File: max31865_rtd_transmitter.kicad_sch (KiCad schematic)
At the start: 4 parts, among them U1 MAX31865xTP

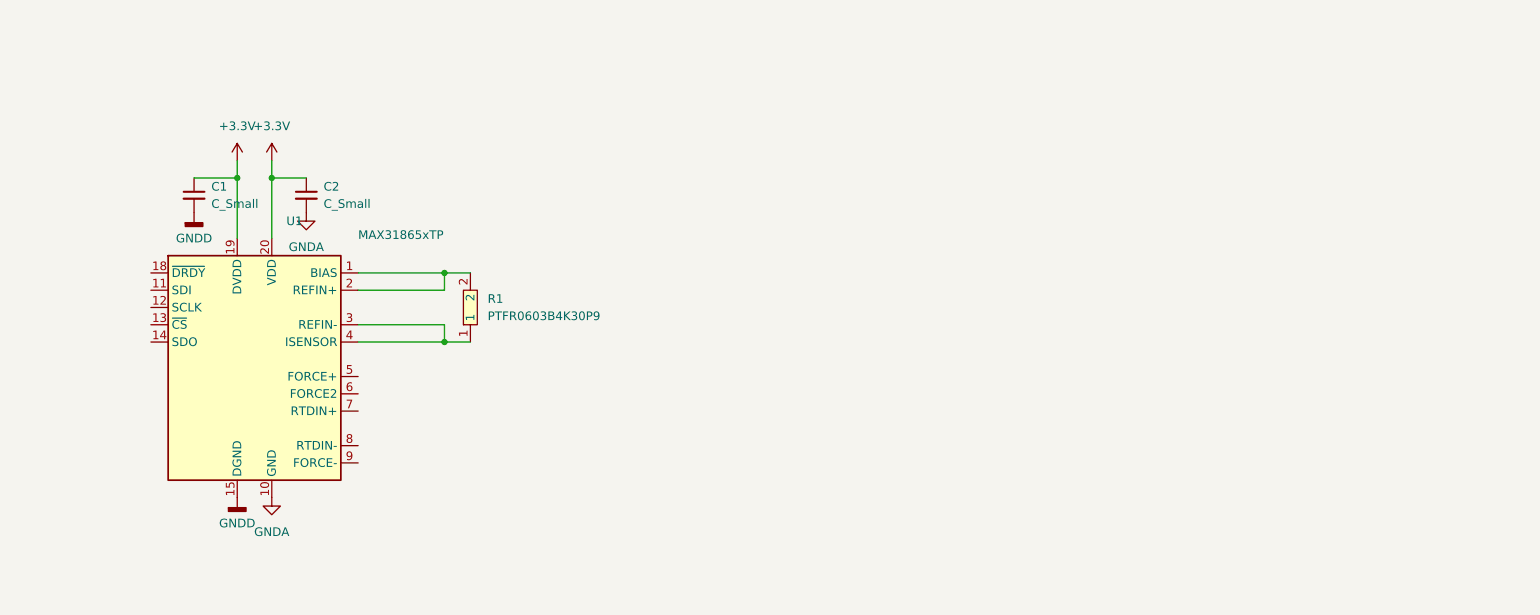
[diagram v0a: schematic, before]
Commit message: Add isolated power and LDO
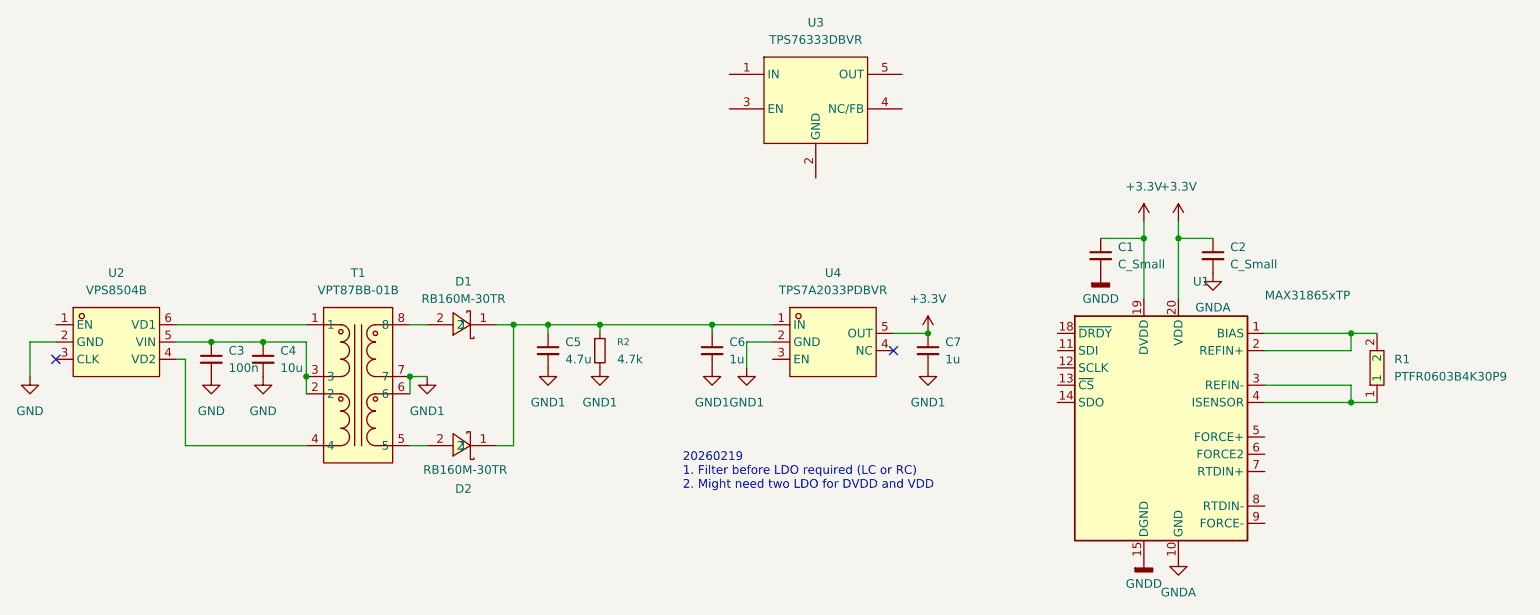
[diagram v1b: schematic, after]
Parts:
- added C3: 100n, symbol Device:C_Small
- added C4: 10u, symbol Device:C_Small
- added C5: 4.7u, symbol Device:C_Small
- added C6, C7: 1u, symbol Device:C_Small
- added D1, D2: RB160M-30TR, rtd-transmitter-library:SOD-123_L2.8-W1.8-LS3.7-RD, symbol rtd-transmitter-library:RB160M-30TR
- added R2: 4.7k, symbol Device:R_Small
- added T1: VPT87BB-01B, rtd-transmitter-library:XFMR-SMD_VPSC_VPT87BB, symbol rtd-transmitter-library:VPT87BB-01B
- added U2: VPS8504B, rtd-transmitter-library:SOT-23-6_L2.9-W1.6-P0.95-LS2.8-BR, symbol rtd-transmitter-library:VPS8504B
- added U3: TPS76333DBVR, rtd-transmitter-library:SOT-23-5_L3.0-W1.7-P0.95-LS2.8-BR, symbol rtd-transmitter-library:TPS76333DBVR
- added U4: TPS7A2033PDBVR, rtd-transmitter-library:SOT-23-5_L2.9-W1.6-P0.95-LS2.8-BR, symbol rtd-transmitter-library:TPS7A2033PDBVR
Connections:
- net +3.3V: now also C7.1, U4.5 (OUT)
- new net: C5.1, C6.1, D1.1, D2.1, R2.1, U4.1 (IN)
- new net: C3.1, C4.1, T1.2, T1.3, U2.5 (VIN)
- new net: T1.1, U2.6 (VD1)
- new net: T1.4, U2.4 (VD2)
- new net: D2.2, T1.5
- new net: D1.2, T1.8
- new net GND: C3.2, C4.2, U2.2 (GND)
- new net GND1: C5.2, C6.2, C7.2, R2.2, T1.6, T1.7, U4.2 (GND)
- no-connect marks 0 -> 2
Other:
- note added: "20260219 1. Filter before LDO required (LC or RC) 2. Might need two LDO for DVDD and VDD"
- moved on the sheet: C1, C2, R1, U1

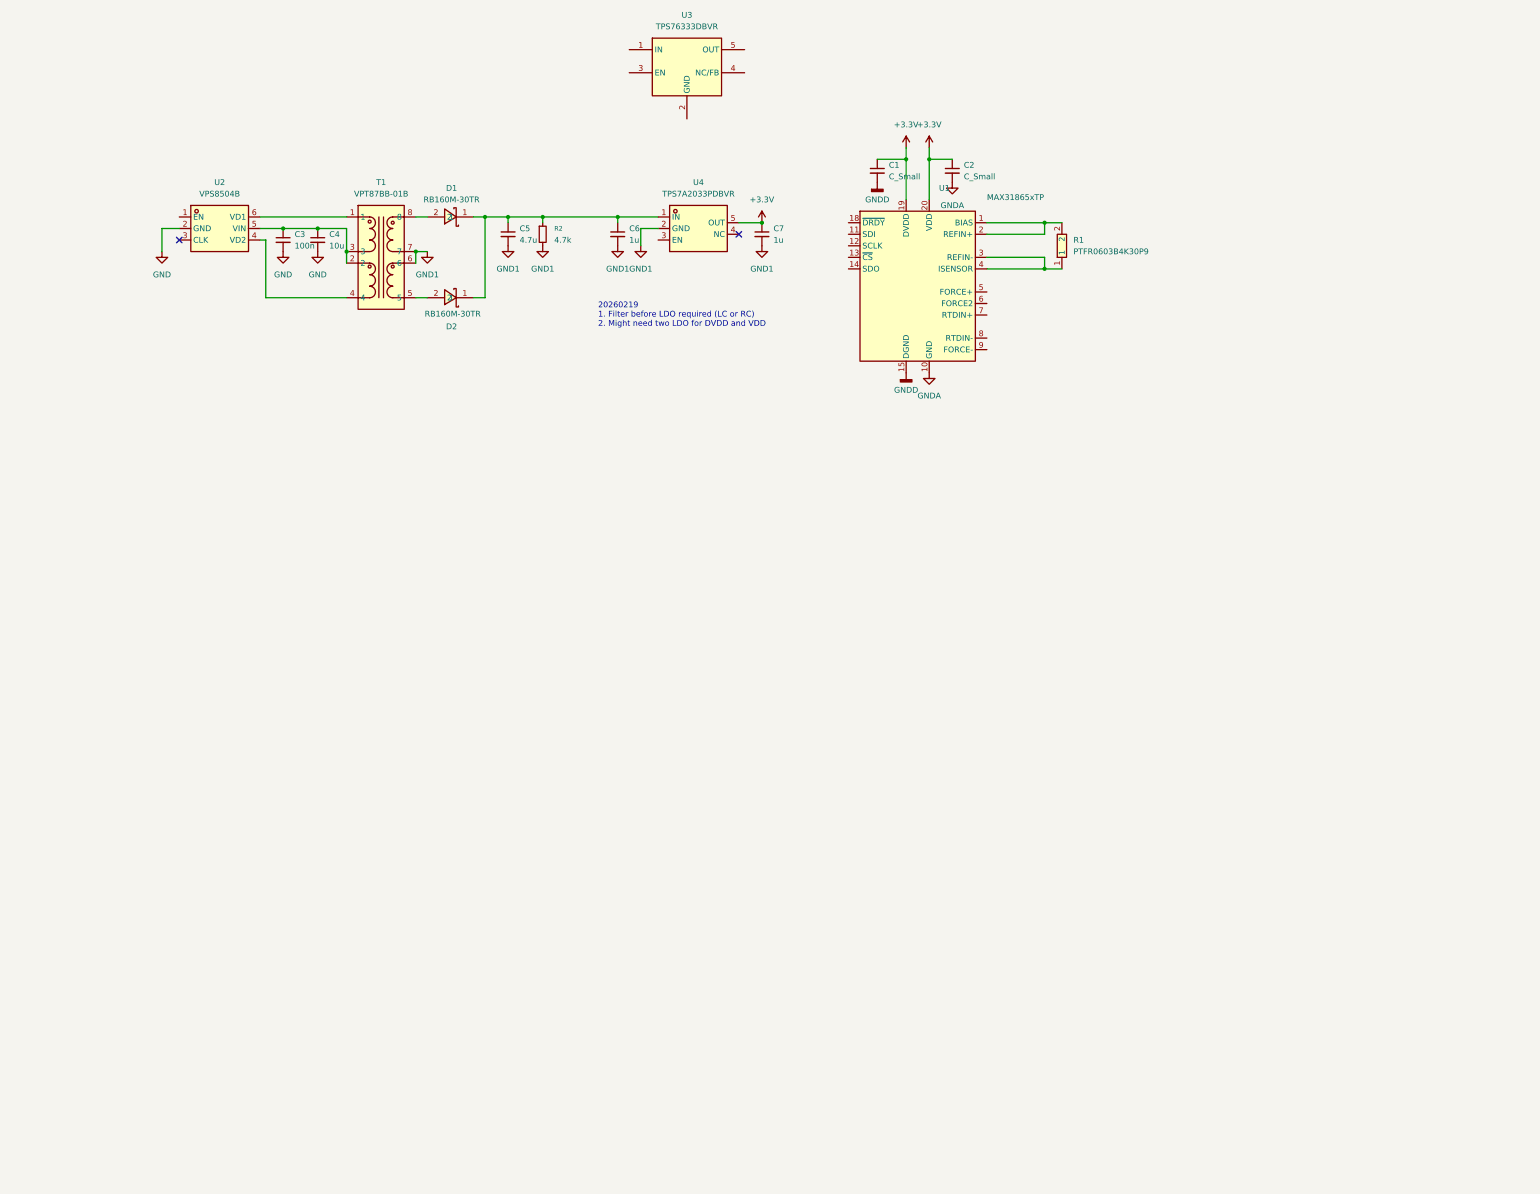
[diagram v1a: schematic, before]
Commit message: Complete single channel design, add rp2350
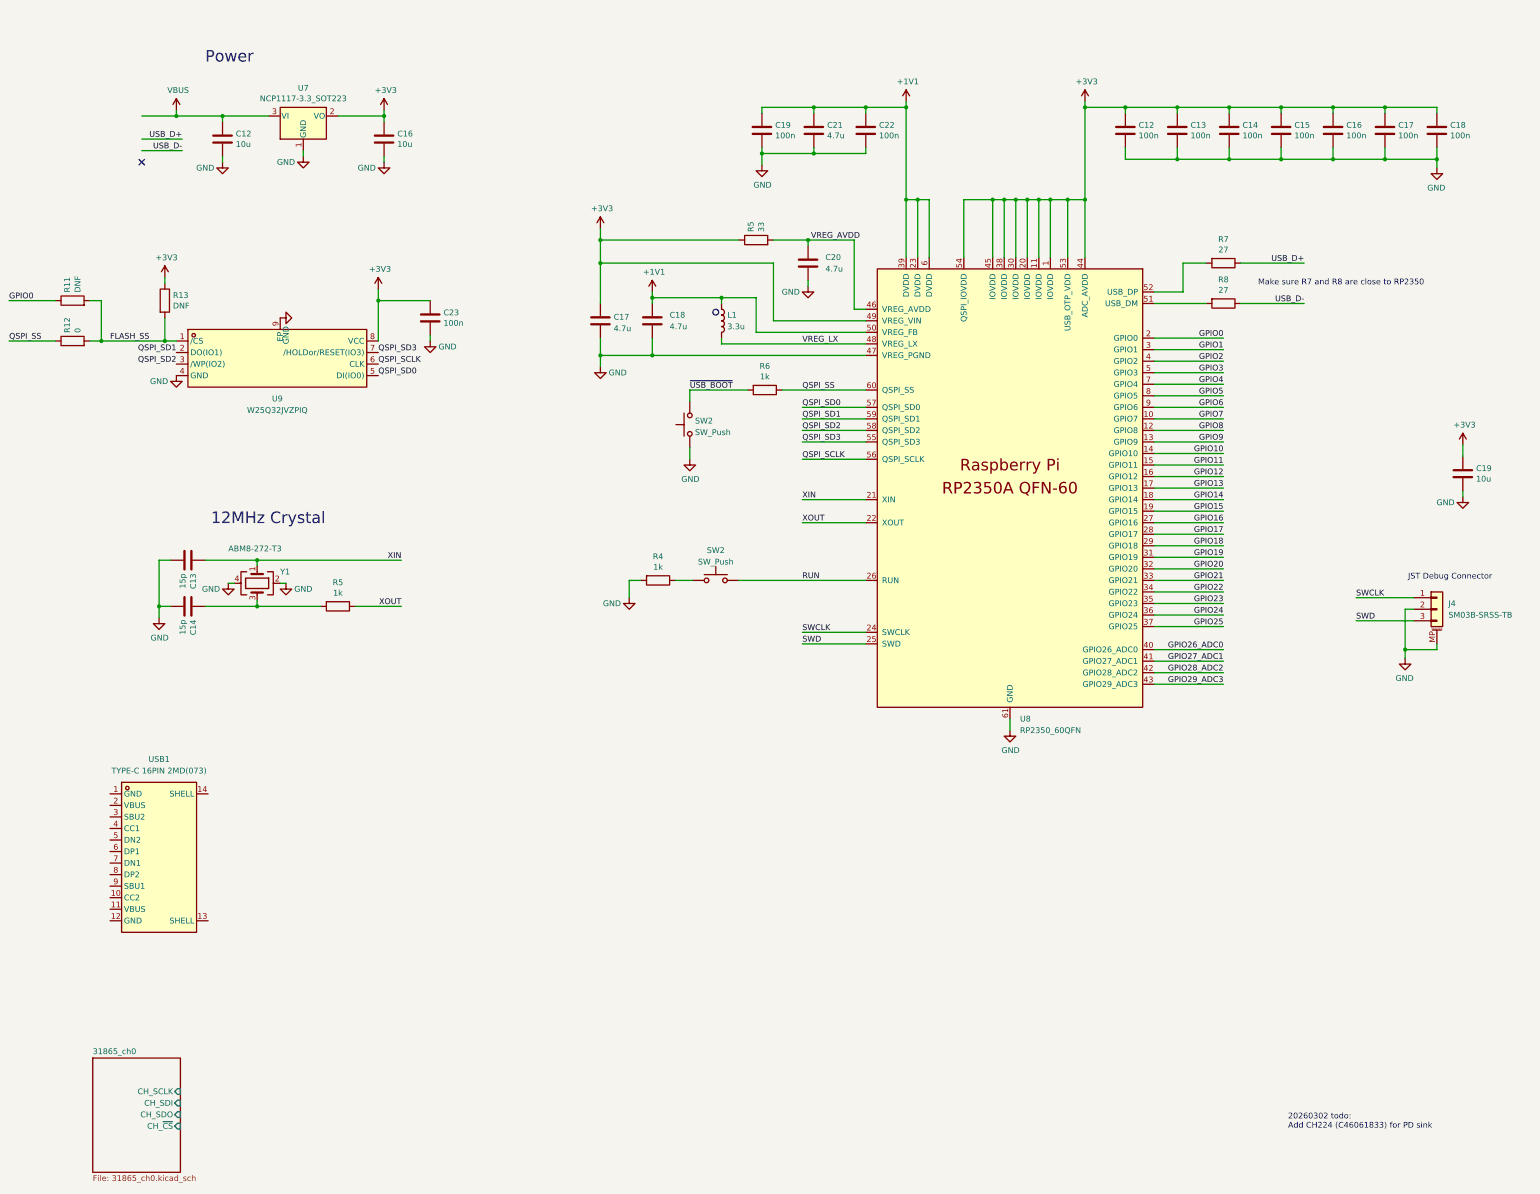
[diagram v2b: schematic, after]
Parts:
- removed C1, C2: C_Small, symbol Device:C_Small
- removed C3: 100n, symbol Device:C_Small
- removed C4: 10u, symbol Device:C_Small
- removed C5: 4.7u, symbol Device:C_Small
- removed C6, C7: 1u, symbol Device:C_Small
- removed D1, D2: RB160M-30TR, rtd-transmitter-library:SOD-123_L2.8-W1.8-LS3.7-RD, symbol rtd-transmitter-library:RB160M-30TR
- removed R1: PTFR0603B4K30P9, rtd-transmitter-library:R0603, symbol rtd-transmitter-library:PTFR0603B4K30P9
- removed R2: 4.7k, symbol Device:R_Small
- removed T1: VPT87BB-01B, rtd-transmitter-library:XFMR-SMD_VPSC_VPT87BB, symbol rtd-transmitter-library:VPT87BB-01B
- removed U1: MAX31865xTP, Package_DFN_QFN:TQFN-20-1EP_5x5mm_P0.65mm_EP3.1x3.1mm_ThermalVias, symbol Sensor_Temperature:MAX31865xTP
- removed U2: VPS8504B, rtd-transmitter-library:SOT-23-6_L2.9-W1.6-P0.95-LS2.8-BR, symbol rtd-transmitter-library:VPS8504B
- removed U3: TPS76333DBVR, rtd-transmitter-library:SOT-23-5_L3.0-W1.7-P0.95-LS2.8-BR, symbol rtd-transmitter-library:TPS76333DBVR
- removed U4: TPS7A2033PDBVR, rtd-transmitter-library:SOT-23-5_L2.9-W1.6-P0.95-LS2.8-BR, symbol rtd-transmitter-library:TPS7A2033PDBVR
- added C12, C13, C14, C15, C16, C17, C18, C19, C22, C23: 100n, Capacitor_SMD:C_0402_1005Metric, symbol Device:C
- added C12, C16, C19: 10u, Capacitor_SMD:C_0805_2012Metric, symbol Device:C
- added C13, C14: 15p, Capacitor_SMD:C_0402_1005Metric, symbol Device:C
- added C17, C18: 4.7u, RP2350_60QFN_minimal:C_0402_1005Metric_small_pads, symbol Device:C
- added C20, C21: 4.7u, Capacitor_SMD:C_0402_1005Metric, symbol Device:C
- added J4: SM03B-SRSS-TB, Connector_JST:JST_SH_SM03B-SRSS-TB_1x03-1MP_P1.00mm_Horizontal, symbol Connector_Generic_MountingPin:Conn_01x03_MountingPin
- added L1: 3.3u, RP2350_60QFN_minimal:L_pol_2016, symbol Device:L
- added R11, R13: DNF, Resistor_SMD:R_0402_1005Metric, symbol Device:R
- added R12: 0, Resistor_SMD:R_0402_1005Metric, symbol Device:R
- added R4, R5, R6: 1k, Resistor_SMD:R_0402_1005Metric, symbol Device:R
- added R5: 33, Resistor_SMD:R_0402_1005Metric, symbol Device:R
- added R7, R8: 27, Resistor_SMD:R_0402_1005Metric, symbol Device:R
- added SW2 (x2): SW_Push, Button_Switch_SMD:SW_Push_1P1T_NO_Vertical_Wuerth_434133025816, symbol Switch:SW_Push
- added U7: NCP1117-3.3_SOT223, Package_TO_SOT_SMD:SOT-223-3_TabPin2, symbol Regulator_Linear:NCP1117-3.3_SOT223
- added U8: RP2350_60QFN, RP2350_60QFN_minimal:RP2350-QFN-60-1EP_7x7_P0.4mm_EP3.4x3.4mm_ThermalVias, symbol MCU_RaspberryPi_RP2350:RP2350_60QFN
- added U9: W25Q32JVZPIQ, rtd-transmitter-library:WSON-8_L6.0-W5.0-P1.27-BL-EP, symbol rtd-transmitter-library:W25Q32JVZPIQ
- added USB1: TYPE-C 16PIN 2MD(073), rtd-transmitter-library:USB-C-SMD_TYPE-C-6PIN-2MD-073, symbol rtd-transmitter-library:TYPE-C16PIN2MD(073)
- added Y1: ABM8-272-T3, Crystal:Crystal_SMD_3225-4Pin_3.2x2.5mm, symbol Device:Crystal_GND24
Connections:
- net GND: now also C12.2, C12.2, C13.2, C13.2, C14.2, C14.2, C15.2, C16.2, C16.2, C17.2, C17.2, C18.2, C18.2, C19.2, C19.2, C20.2, C21.2, C22.2, C23.2, J4.2 (Pin_2), J4.MP (MountPin), R4.2, SW2.1, U7.1 (GND), U8.47 (VREG_PGND), U8.61 (GND), U9.4 (GND), U9.9 (EP), Y1.2, Y1.4
- new net: R7.2, U8.52 (USB_DP)
- new net: R8.2, U8.51 (USB_DM)
- new net: C14.1, R5.2, Y1.3
- new net: R4.1, SW2.1
- new net +1V1: C18.1, C19.1, C21.1, C22.1, L1.1, U8.23 (DVDD), U8.39 (DVDD), U8.50 (VREG_FB), U8.6 (DVDD)
- new net +3V3: C12.1, C13.1, C14.1, C15.1, C16.1, C16.1, C17.1, C17.1, C18.1, C19.1, C23.1, R13.1, R5.1, U7.2 (VO), U8.1 (IOVDD), U8.11 (IOVDD), U8.20 (IOVDD), U8.30 (IOVDD), U8.38 (IOVDD), U8.44 (ADC_AVDD), U8.45 (IOVDD), U8.49 (VREG_VIN), U8.53 (USB_OTP_VDD), U8.54 (QSPI_IOVDD), U9.8 (VCC)
- new net FLASH_SS: R11.2, R12.2, R13.2, U9.1 (/CS)
- new net GPIO0: R11.1, U8.2 (GPIO0)
- new net GPIO1: U8.3 (GPIO1)
- new net GPIO10: U8.14 (GPIO10)
- new net GPIO11: U8.15 (GPIO11)
- new net GPIO12: U8.16 (GPIO12)
- new net GPIO13: U8.17 (GPIO13)
- new net GPIO14: U8.18 (GPIO14)
- new net GPIO15: U8.19 (GPIO15)
- new net GPIO16: U8.27 (GPIO16)
- new net GPIO17: U8.28 (GPIO17)
- new net GPIO18: U8.29 (GPIO18)
- new net GPIO19: U8.31 (GPIO19)
- new net GPIO2: U8.4 (GPIO2)
- new net GPIO20: U8.32 (GPIO20)
- new net GPIO21: U8.33 (GPIO21)
- new net GPIO22: U8.34 (GPIO22)
- new net GPIO23: U8.35 (GPIO23)
- new net GPIO24: U8.36 (GPIO24)
- new net GPIO25: U8.37 (GPIO25)
- new net GPIO26_ADC0: U8.40 (GPIO26_ADC0)
- new net GPIO27_ADC1: U8.41 (GPIO27_ADC1)
- new net GPIO28_ADC2: U8.42 (GPIO28_ADC2)
- new net GPIO29_ADC3: U8.43 (GPIO29_ADC3)
- new net GPIO3: U8.5 (GPIO3)
- new net GPIO4: U8.7 (GPIO4)
- new net GPIO5: U8.8 (GPIO5)
- new net GPIO6: U8.9 (GPIO6)
- new net GPIO7: U8.10 (GPIO7)
- new net GPIO8: U8.12 (GPIO8)
- new net GPIO9: U8.13 (GPIO9)
- new net QSPI_SCLK: U8.56 (QSPI_SCLK), U9.6 (CLK)
- new net QSPI_SD0: U8.57 (QSPI_SD0), U9.5 (DI(IO0))
- new net QSPI_SD1: U8.59 (QSPI_SD1), U9.2 (DO(IO1))
- new net QSPI_SD2: U8.58 (QSPI_SD2), U9.3 (/WP(IO2))
- new net QSPI_SD3: U8.55 (QSPI_SD3), U9.7 (/HOLDor/RESET(IO3))
- new net QSPI_SS: R12.1, R6.1, U8.60 (QSPI_SS)
- new net RUN: SW2.2, U8.26 (RUN)
- new net SWCLK: J4.1 (Pin_1), U8.24 (SWCLK)
- new net SWD: J4.3 (Pin_3), U8.25 (SWD)
- new net USB_D+: R7.1
- new net USB_D-: R8.1
- new net VBUS: C12.1, U7.3 (VI)
- new net VREG_AVDD: C20.1, R5.2, U8.46 (VREG_AVDD)
- new net VREG_LX: L1.2, U8.48 (VREG_LX)
- new net XIN: C13.1, U8.21 (XIN), Y1.1
- new net XOUT: R5.1, U8.22 (XOUT)
- new net ~{USB_BOOT}: R6.2, SW2.2
- no-connect marks 2 -> 1
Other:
- added sheet 31865_ch0 (31865_ch0.kicad_sch)
- note added: "12MHz Crystal"
- note added: "20260302 todo: Add CH224 (C46061833) for PD sink"
- note added: "JST Debug Connector"
- note added: "Make sure R7 and R8 are close to RP2350"
- note added: "Power"
- note removed: "20260219 1. Filter before LDO required (LC or RC) 2. Might need two LDO for DVDD and VDD"

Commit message: complete schematic layout
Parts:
- removed C12, C13, C14, C15, C16, C17, C18, C19, C22, C23: 100n, Capacitor_SMD:C_0402_1005Metric, symbol Device:C
- removed C12, C16, C19: 10u, Capacitor_SMD:C_0805_2012Metric, symbol Device:C
- removed C13, C14: 15p, Capacitor_SMD:C_0402_1005Metric, symbol Device:C
- removed C17, C18: 4.7u, RP2350_60QFN_minimal:C_0402_1005Metric_small_pads, symbol Device:C
- removed C20, C21: 4.7u, Capacitor_SMD:C_0402_1005Metric, symbol Device:C
- removed J4: SM03B-SRSS-TB, Connector_JST:JST_SH_SM03B-SRSS-TB_1x03-1MP_P1.00mm_Horizontal, symbol Connector_Generic_MountingPin:Conn_01x03_MountingPin
- removed L1: 3.3u, RP2350_60QFN_minimal:L_pol_2016, symbol Device:L
- removed R11, R13: DNF, Resistor_SMD:R_0402_1005Metric, symbol Device:R
- removed R12: 0, Resistor_SMD:R_0402_1005Metric, symbol Device:R
- removed R4, R5, R6: 1k, Resistor_SMD:R_0402_1005Metric, symbol Device:R
- removed R5: 33, Resistor_SMD:R_0402_1005Metric, symbol Device:R
- removed R7, R8: 27, Resistor_SMD:R_0402_1005Metric, symbol Device:R
- removed SW2 (x2): SW_Push, Button_Switch_SMD:SW_Push_1P1T_NO_Vertical_Wuerth_434133025816, symbol Switch:SW_Push
- removed U7: NCP1117-3.3_SOT223, Package_TO_SOT_SMD:SOT-223-3_TabPin2, symbol Regulator_Linear:NCP1117-3.3_SOT223
- removed U8: RP2350_60QFN, RP2350_60QFN_minimal:RP2350-QFN-60-1EP_7x7_P0.4mm_EP3.4x3.4mm_ThermalVias, symbol MCU_RaspberryPi_RP2350:RP2350_60QFN
- removed U9: W25Q32JVZPIQ, rtd-transmitter-library:WSON-8_L6.0-W5.0-P1.27-BL-EP, symbol rtd-transmitter-library:W25Q32JVZPIQ
- removed USB1: TYPE-C 16PIN 2MD(073), rtd-transmitter-library:USB-C-SMD_TYPE-C-6PIN-2MD-073, symbol rtd-transmitter-library:TYPE-C16PIN2MD(073)
- removed Y1: ABM8-272-T3, Crystal:Crystal_SMD_3225-4Pin_3.2x2.5mm, symbol Device:Crystal_GND24
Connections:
- no-connect marks 1 -> 0
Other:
- added sheet 31865_ch1 (31865_ch0.kicad_sch)
- added sheet 31865_ch2 (31865_ch0.kicad_sch)
- added sheet 31865_ch3 (31865_ch0.kicad_sch)
- added sheet rp2350 (rp2350.kicad_sch)
- note removed: "12MHz Crystal"
- note removed: "JST Debug Connector"
- note removed: "Make sure R7 and R8 are close to RP2350"
- note removed: "Power"
